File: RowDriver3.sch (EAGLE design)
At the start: 25 parts, among them Q1 DPBT8105, Q2 DPBT8105, Q3 DPBT8105, Q4 DPBT8105

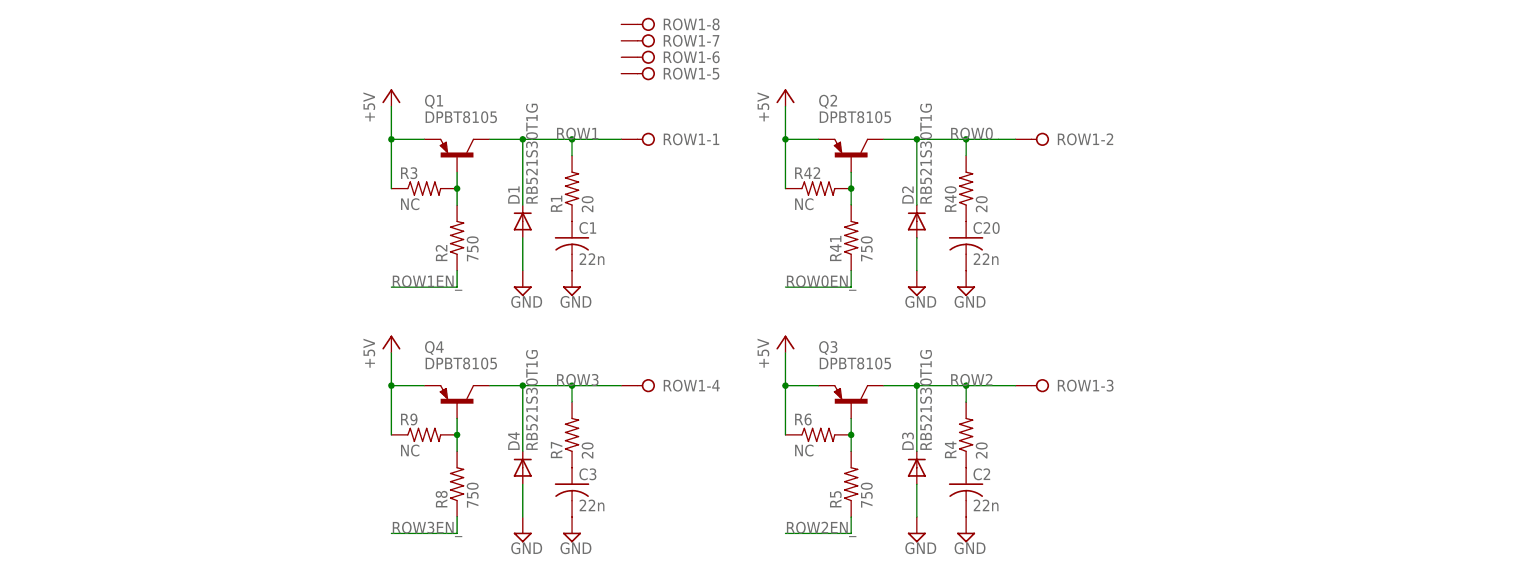
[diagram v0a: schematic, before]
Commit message: Created initial main board. Created layout for row driver, and tiled it. The new board and schematic files for the row driver are intermediate steps.
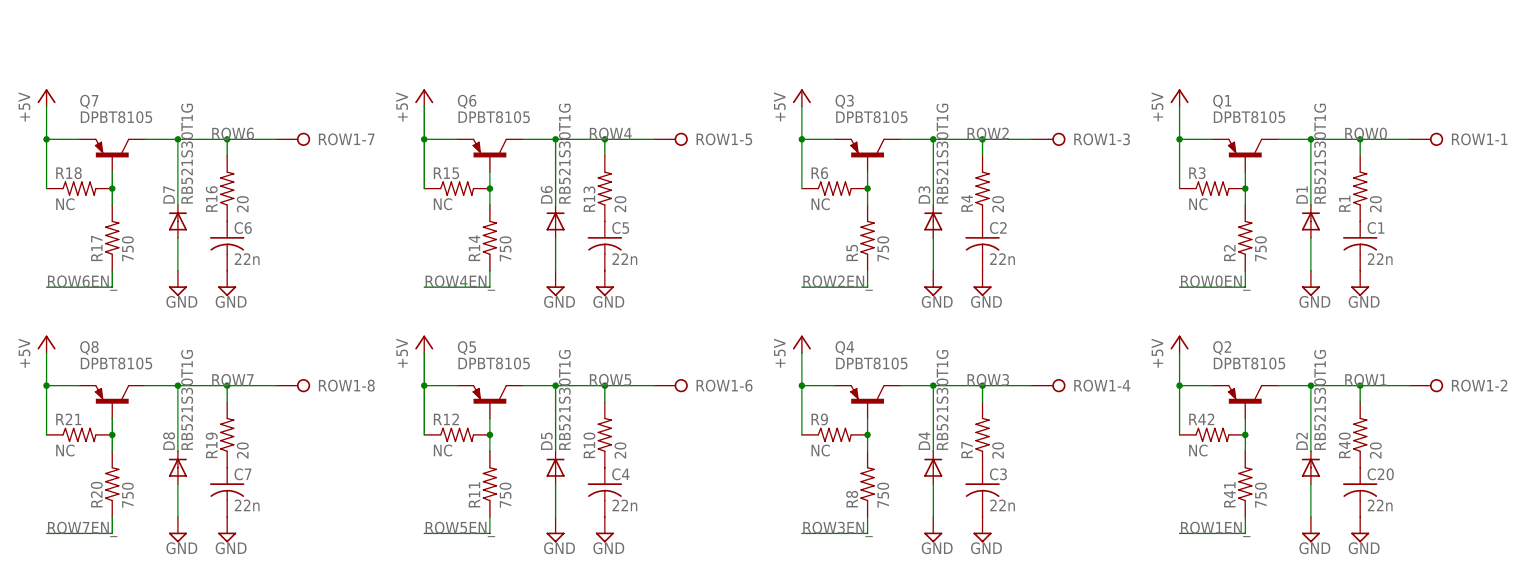
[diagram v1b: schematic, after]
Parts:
- added C4, C5, C6, C7: 22n, resistor:C-USC0603
- added D5, D6, D7, D8: RB521S30T1G, diode:DIODE-SOD523
- added Q5, Q6, Q7, Q8: DPBT8105, Parts:DPBT8105
- added R10, R13, R16, R19: 20, resistor:R-US_R0603
- added R11, R14, R17, R20: 750, resistor:R-US_R0603
- added R12, R15, R18, R21: NC, resistor:R-US_R0603
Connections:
- new net N$10: C5.1, R13.1
- new net N$11: Q7.B, R17.2, R18.2
- new net N$12: C6.1, R16.1
- new net N$13: Q8.B, R20.2, R21.2
- new net N$14: C7.1, R19.1
- new net N$7: Q5.B, R11.2, R12.2
- new net N$8: C4.1, R10.1
- new net N$9: Q6.B, R14.2, R15.2
- new net ROW4: D6.C, Q6.C, R13.2, ROW1-5.KL
- new net ROW4EN_: R14.1
- new net ROW5: D5.C, Q5.C, R10.2, ROW1-6.KL
- new net ROW5EN_: R11.1
- new net ROW6: D7.C, Q7.C, R16.2, ROW1-7.KL
- new net ROW6EN_: R17.1
- new net ROW7: D8.C, Q8.C, R19.2, ROW1-8.KL
- new net ROW7EN_: R20.1
- net +5V: now also Q5.E, Q6.E, Q7.E, Q8.E, R12.1, R15.1, R18.1, R21.1
- net GND: now also C4.2, C5.2, C6.2, C7.2, D5.A, D6.A, D7.A, D8.A
- net ROW0: now also D1.C, Q1.C, R1.2, ROW1-1.KL; no longer D2.C, Q2.C, R40.2, ROW1-2.KL
- net ROW0EN_: now also R2.1; no longer R41.1
- net ROW1: now also D2.C, Q2.C, R40.2, ROW1-2.KL; no longer D1.C, Q1.C, R1.2, ROW1-1.KL
- net ROW1EN_: now also R41.1; no longer R2.1
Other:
- moved on the sheet: C1, C2, C20, C3, D1, D2, D3, D4, Q1, Q2, Q3, Q4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
